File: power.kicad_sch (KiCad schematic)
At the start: 35 parts, among them J1 Conn_01x03_Male, Q1 DMG9926UDM, U1 MAX17048G+T10, U2 MAX8903AETI+T, U3 BQ29728DSER, U4 XC6210B332MR

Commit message: ci: prepare files for CI
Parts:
- L1: footprint Inductor_SMD:L_Vishay_IFSC-1515AH_4x4x1.8mm -> Gigahawk:L_Vishay_IFSC-1515AH_4x4x1.8mm
- U1: footprint Package_DFN_QFN:DFN-8-1EP_2x2mm_P0.5mm_EP0.6x1.2mm -> Gigahawk:DFN-8-1EP_2x2mm_P0.5mm_EP0.6x1.2mm
- U2: footprint Package_DFN_QFN:QFN-28-1EP_4x4mm_P0.4mm_EP2.6x2.6mm -> Gigahawk:QFN-28-1EP_4x4mm_P0.4mm_EP2.6x2.6mm
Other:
- title: (none) -> piPod IO/SMC Board
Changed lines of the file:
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@@
 (kicad_sch (version 20211123) (generator eeschema)
   (paper "A4")
+  (title_block
+    (title "piPod IO/SMC Board")
+    (date "${DATE}")
+    (rev "%{TAG} (${REVISION})")
+  )
   (junction (at 215.9 76.2) (diameter 0) (color 0 0 0 0)
   )
@@
     (property "Reference" "U2" (id 0) (at 113.03 33.02 0))
     (property "Value" "MAX8903AETI+T" (id 1) (at 113.03 35.56 0))
-    (property "Footprint" "Package_DFN_QFN:QFN-28-1EP_4x4mm_P0.4mm_EP2.6x2.6mm" (id 2) (at 113.03 52.07 0)
+    (property "Footprint" "Gigahawk:QFN-28-1EP_4x4mm_P0.4mm_EP2.6x2.6mm" (id 2) (at 113.03 52.07 0)
       (effects (font (size 1.27 1.27)) (justify left bottom) hide)
     )
@@
     (property "Reference" "L1" (id 0) (at 110.49 87.63 90))
     (property "Value" "1u" (id 1) (at 110.49 90.17 90))
-    (property "Footprint" "Inductor_SMD:L_Vishay_IFSC-1515AH_4x4x1.8mm" (id 2) (at 110.49 86.36 0)
+    (property "Footprint" "Gigahawk:L_Vishay_IFSC-1515AH_4x4x1.8mm" (id 2) (at 110.49 86.36 0)
       (effects (font (size 1.27 1.27)) hide)
     )
@@
     (property "Reference" "U1" (id 0) (at 62.865 147.32 0))
     (property "Value" "MAX17048G+T10" (id 1) (at 62.865 149.86 0))
-    (property "Footprint" "Package_DFN_QFN:DFN-8-1EP_2x2mm_P0.5mm_EP0.6x1.2mm" (id 2) (at 62.865 172.72 0)
-      (effects (font (size 1.27 1.27)) hide)
-    )
+    (property "Footprint" "Gigahawk:DFN-8-1EP_2x2mm_P0.5mm_EP0.6x1.2mm" (id 2) (at 62.865 172.72 0)
+      (effects (font (size 1.27 1.27)) hide)
+    )

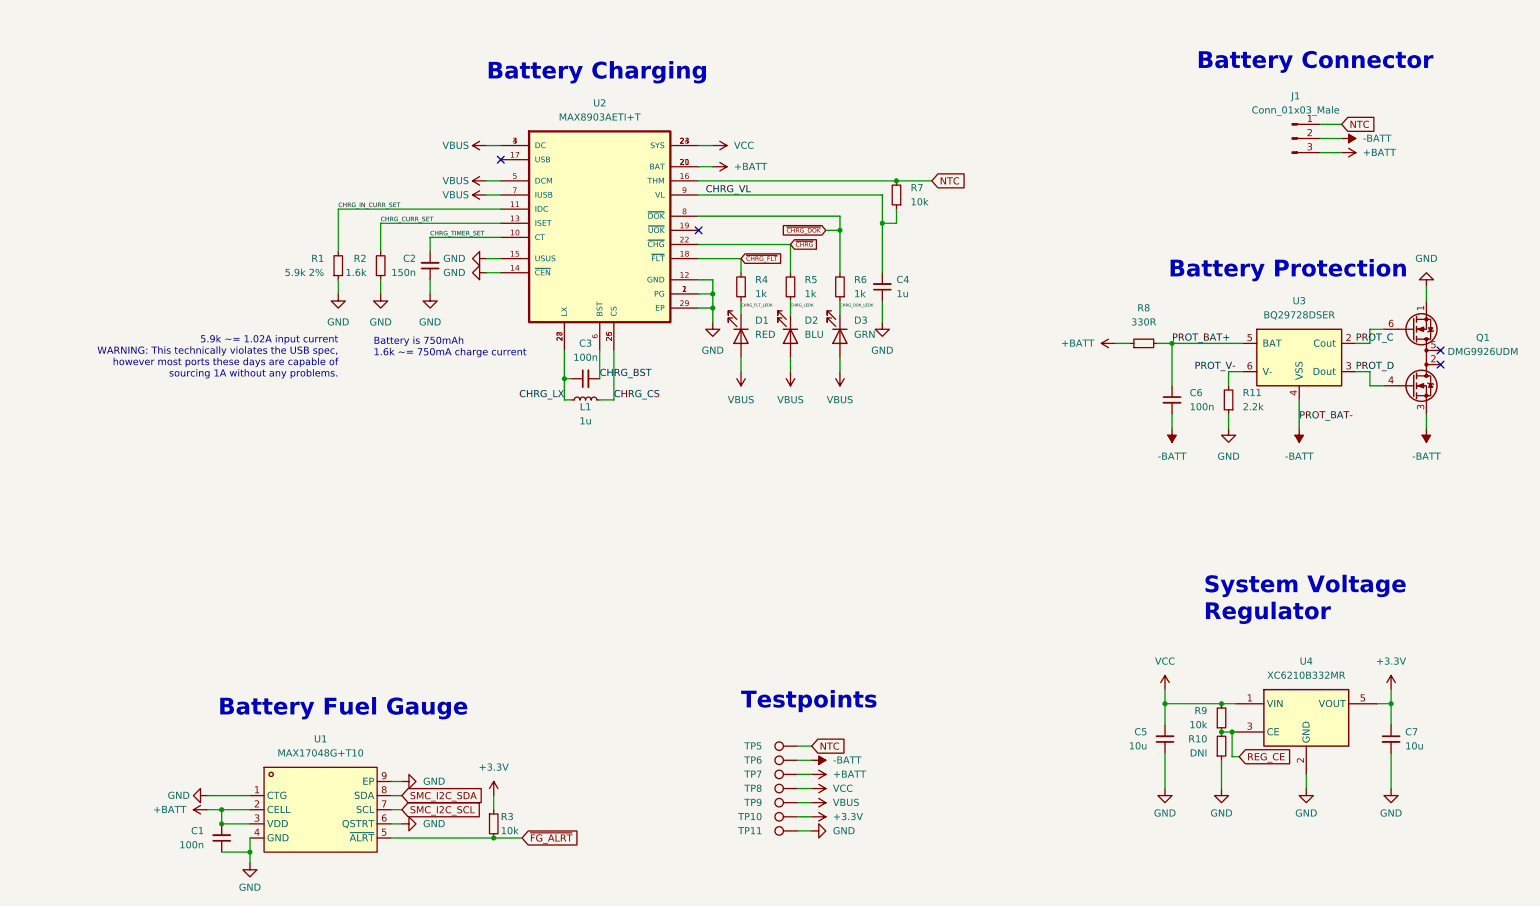
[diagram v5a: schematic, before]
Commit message: ci: test marking parts in sch for bom
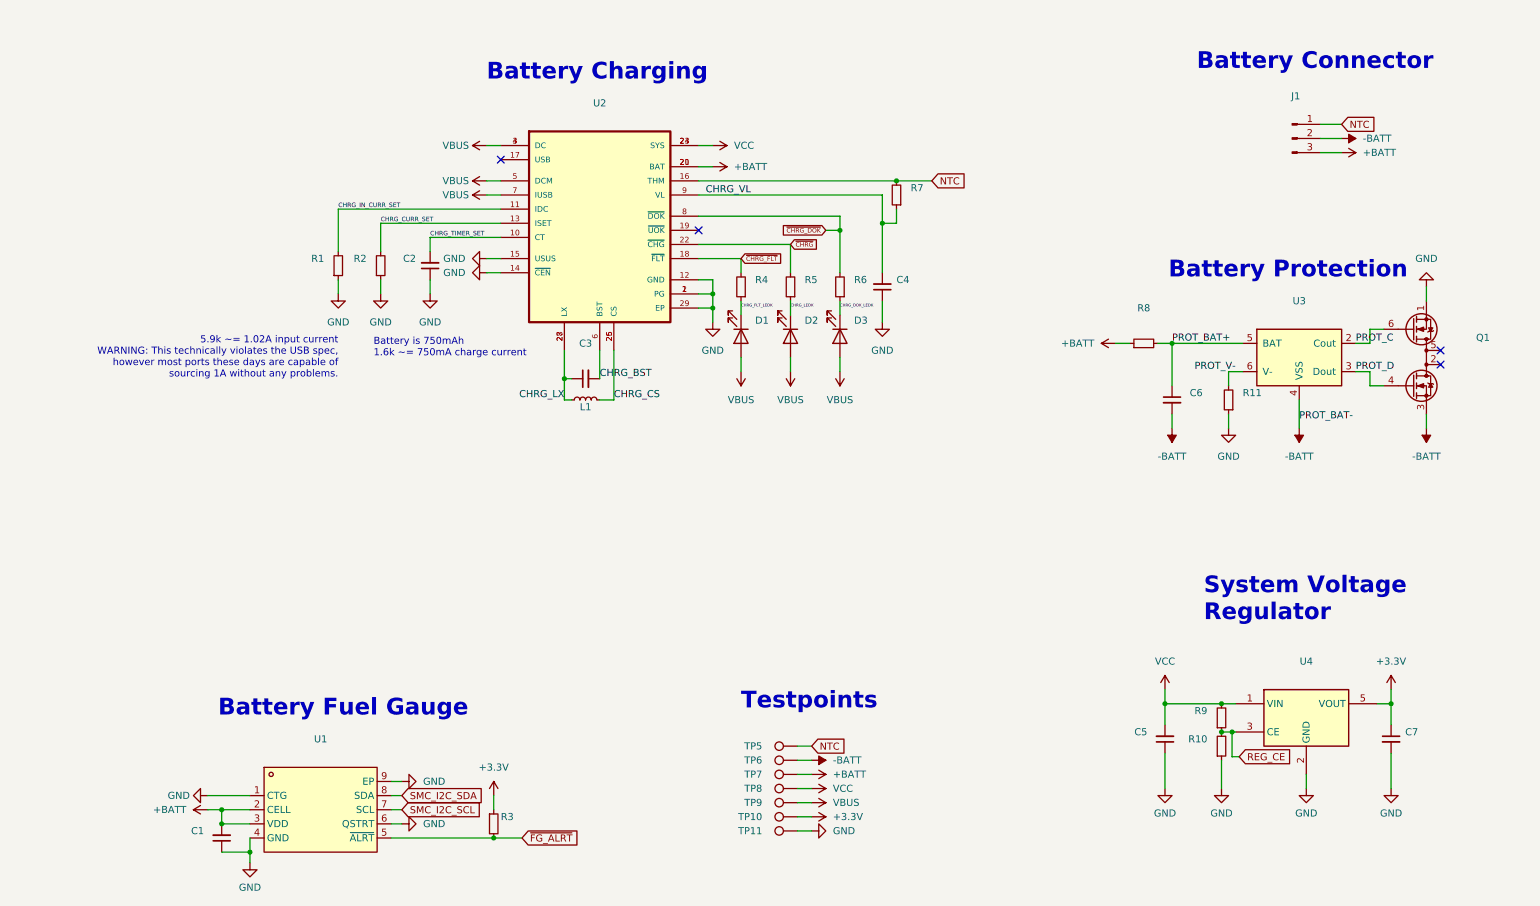
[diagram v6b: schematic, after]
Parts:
- C1, C3, C6: value 100n -> (none); footprint Capacitor_SMD:C_0402_1005Metric -> (none)
- C2: value 150n -> (none); footprint Capacitor_SMD:C_0402_1005Metric -> (none)
- C4: value 1u -> (none); footprint Capacitor_SMD:C_0402_1005Metric -> (none)
- C5, C7: value 10u -> (none); footprint Capacitor_SMD:C_0402_1005Metric -> (none)
- D1: value RED -> (none); footprint LED_SMD:LED_0402_1005Metric -> (none)
- D2: value BLU -> (none); footprint LED_SMD:LED_0402_1005Metric -> (none)
- D3: value GRN -> (none); footprint LED_SMD:LED_0402_1005Metric -> (none)
- J1: value Conn_01x03_Male -> (none); footprint Gigahawk:Molex_PicoBlade_53047-0310_1x03_P1.25mm_Vertical -> (none)
- L1: value 1u -> (none); footprint Gigahawk:L_Vishay_IFSC-1515AH_4x4x1.8mm -> (none)
- Q1: value DMG9926UDM -> (none); footprint Package_TO_SOT_SMD:SOT-23-6 -> (none)
- R1: value 5.9k 2% -> (none); footprint Resistor_SMD:R_0402_1005Metric -> (none)
- R10: value DNI -> (none); footprint Resistor_SMD:R_0402_1005Metric -> (none)
- R11: value 2.2k -> (none); footprint Resistor_SMD:R_0402_1005Metric -> (none)
- R2: value 1.6k -> (none); footprint Resistor_SMD:R_0402_1005Metric -> (none)
- R3, R7, R9: value 10k -> (none); footprint Resistor_SMD:R_0402_1005Metric -> (none)
- R4, R5, R6: value 1k -> (none); footprint Resistor_SMD:R_0402_1005Metric -> (none)
- R8: value 330R -> (none); footprint Resistor_SMD:R_0402_1005Metric -> (none)
- TP10, TP11, TP5, TP6, TP7, TP8, TP9: value TestPoint -> (none); footprint TestPoint:TestPoint_Pad_D1.5mm -> (none)
- U1: value MAX17048G+T10 -> (none); footprint Gigahawk:DFN-8-1EP_2x2mm_P0.5mm_EP0.6x1.2mm -> (none)
- U2: value MAX8903AETI+T -> (none); footprint Gigahawk:QFN-28-1EP_4x4mm_P0.4mm_EP2.6x2.6mm -> (none)
- U3: value BQ29728DSER -> (none); footprint Package_SON:WSON-6_1.5x1.5mm_P0.5mm -> (none)
- U4: value XC6210B332MR -> (none); footprint Package_TO_SOT_SMD:SOT-23-5 -> (none)
